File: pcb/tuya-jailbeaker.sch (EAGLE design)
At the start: 17 parts, among them U1 ESP8285, X1 26MHz

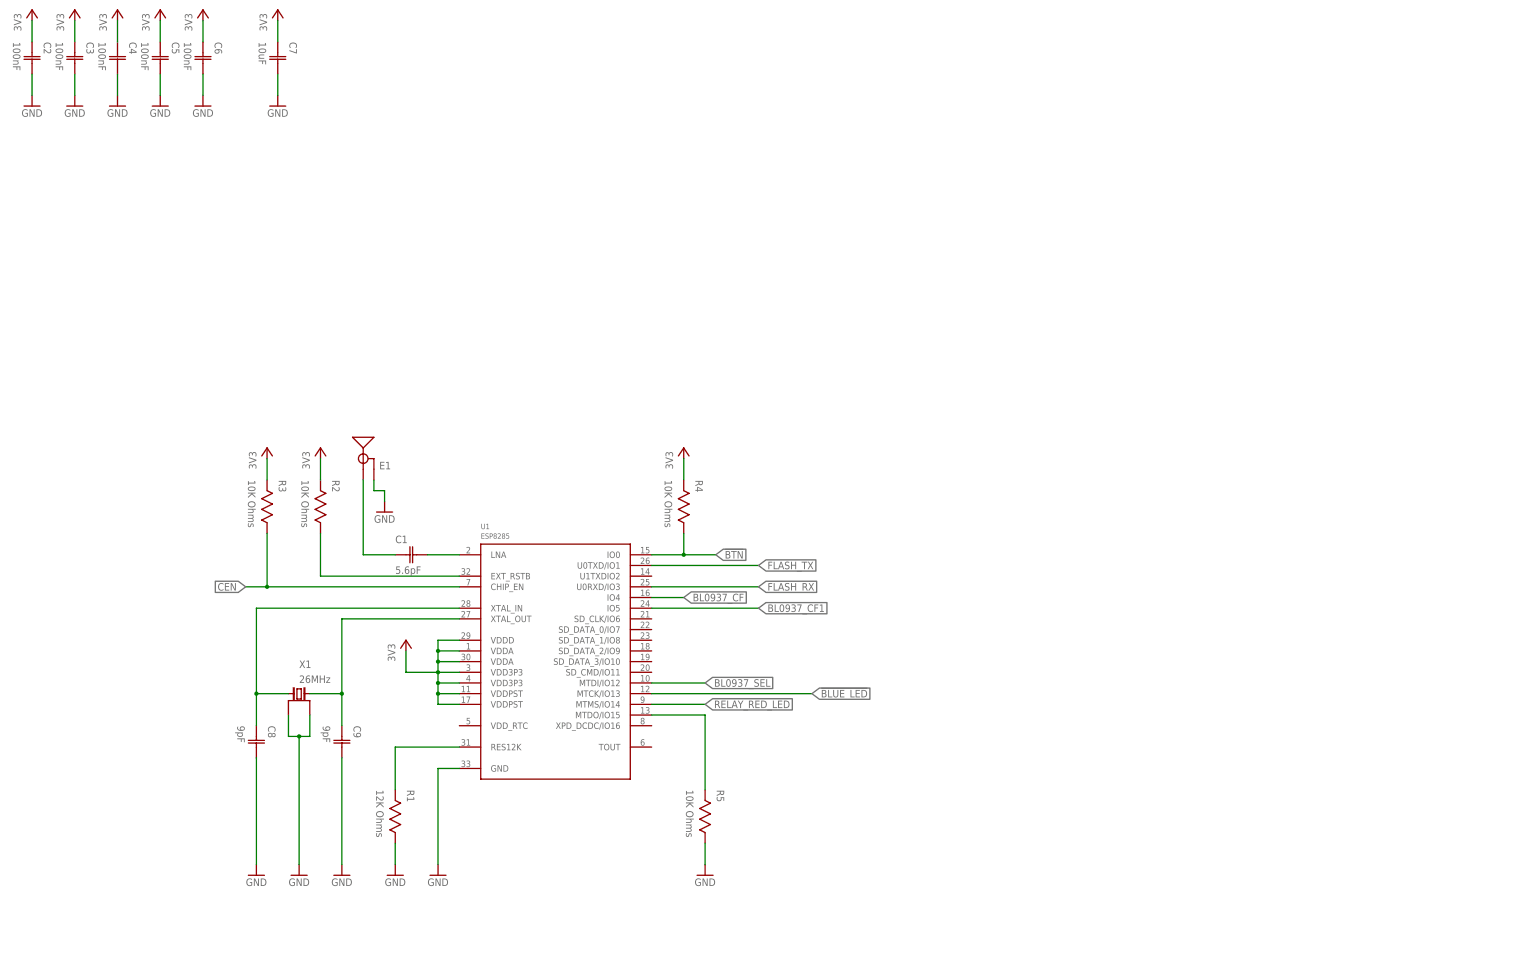
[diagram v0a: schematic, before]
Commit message: Add logo Generate schematic PDF
Signed-off-by: João Silva <jgc3silva@gmail.com>
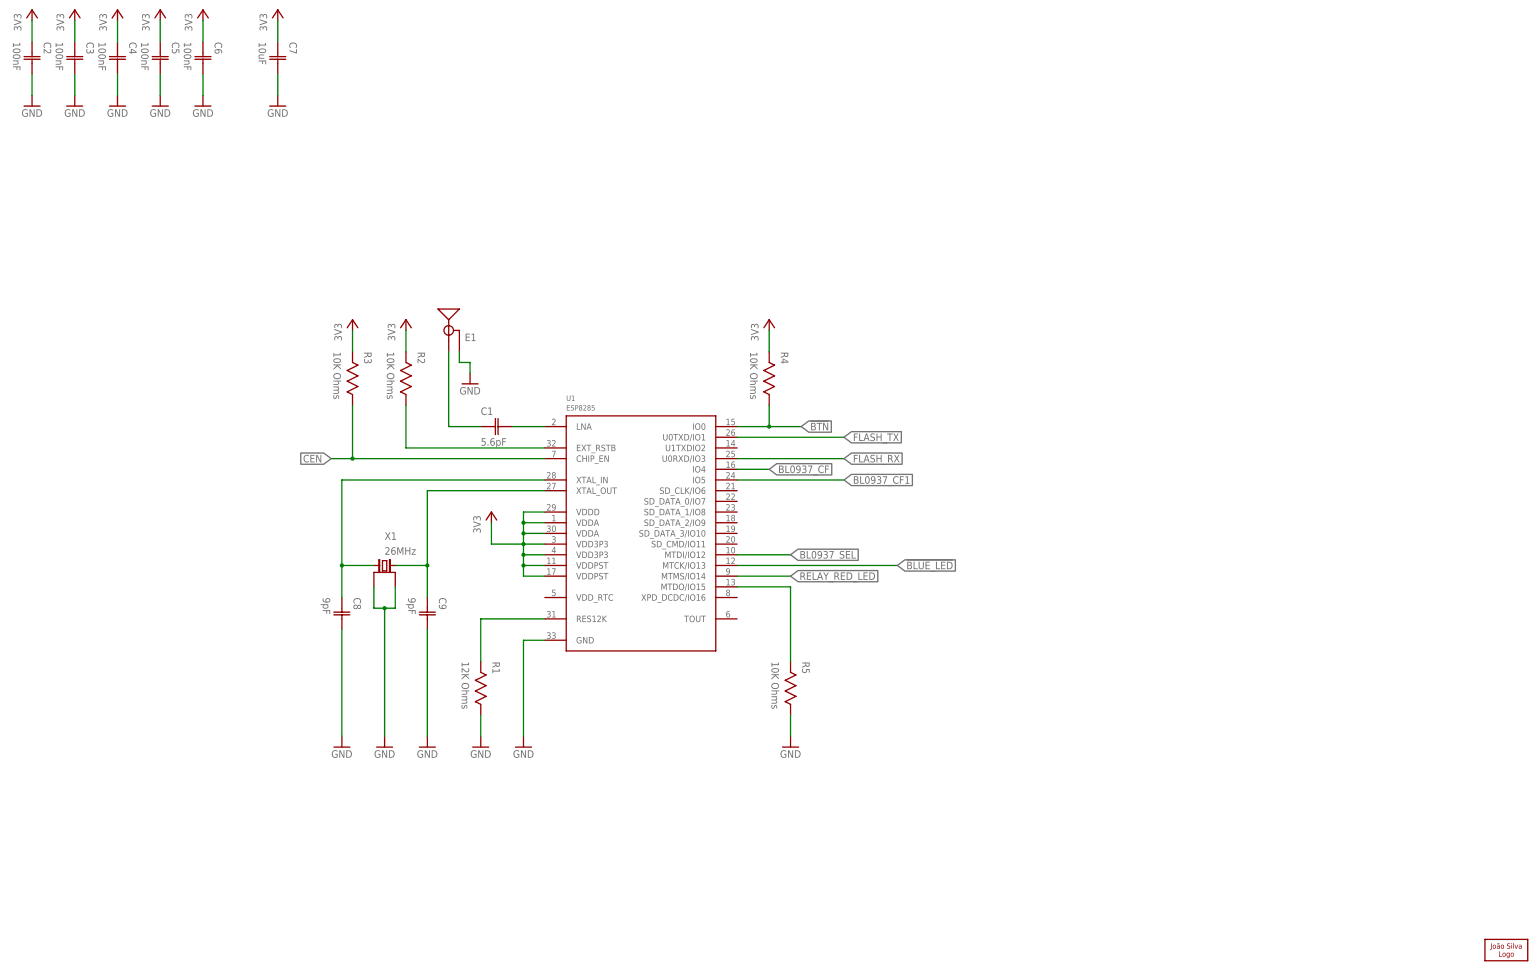
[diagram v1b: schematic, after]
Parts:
- added LOGO1: JS-5MM, Silkscreen:JS-5MM
- X1: OCLCSC (none) -> C709005
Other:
- moved on the sheet: C1, C8, C9, E1, R1, R2, R3, R4, R5, U1, X1

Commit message: Update to ESP32-C3
Signed-off-by: João Silva <jgc3silva@gmail.com>
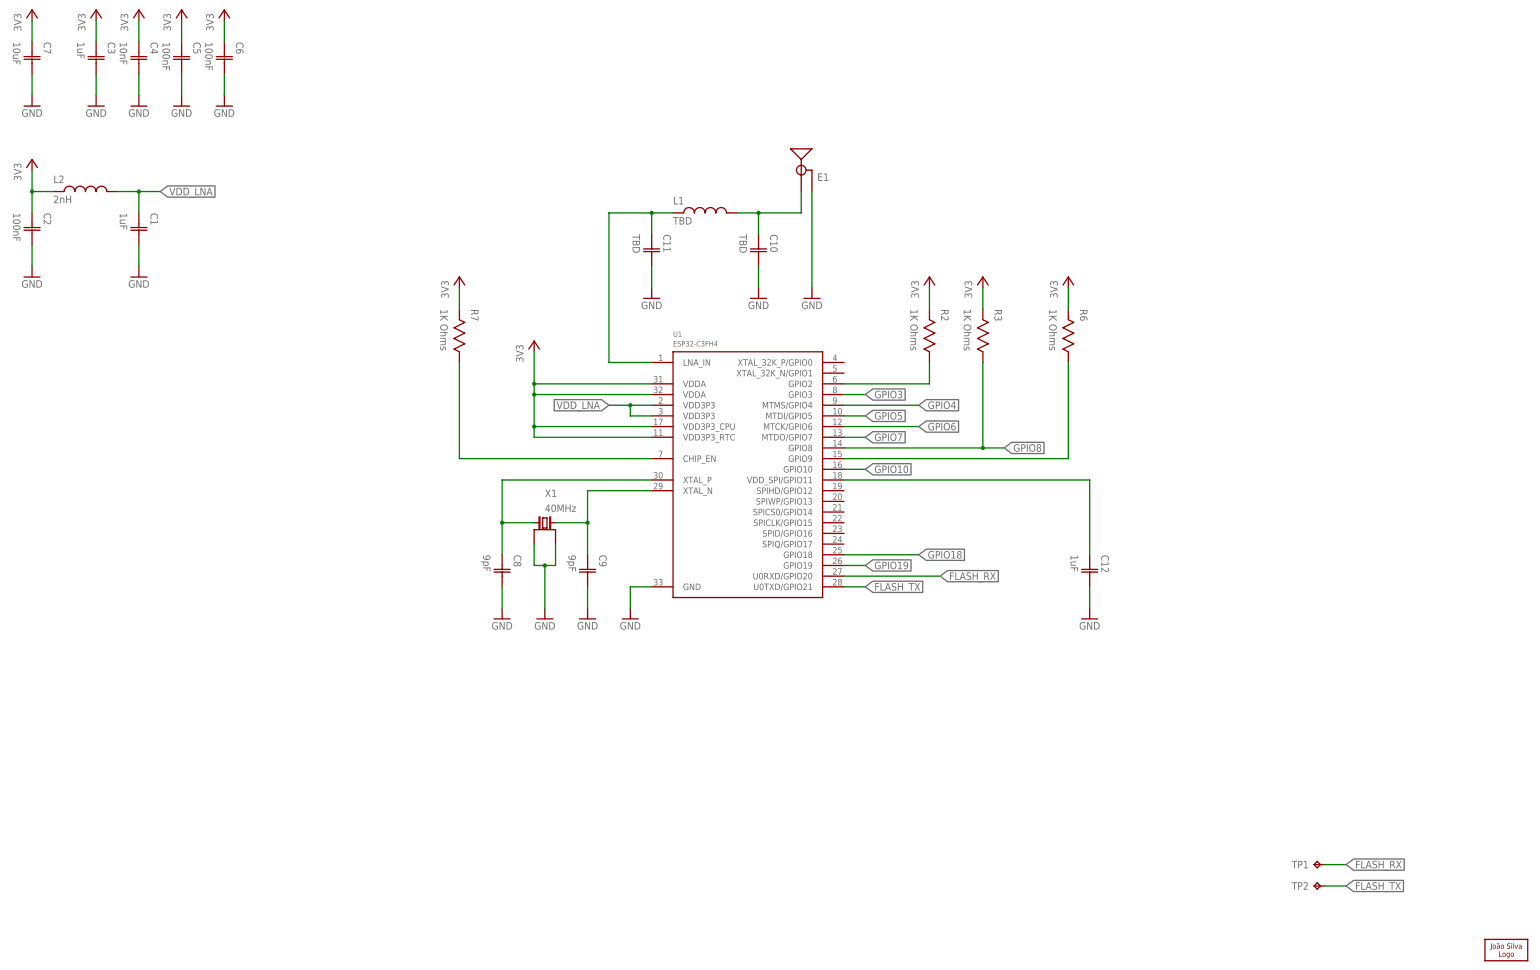
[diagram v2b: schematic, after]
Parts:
- removed R1: 12K Ohms, Resistor:RESISTOR-0201
- removed R4, R5: 10K Ohms, Resistor:RESISTOR-0201
- added C10, C11: TBD, Capacitor:CAPACITOR-0402
- added C12: 1uF, Capacitor:CAPACITOR-0402
- added L1: TBD, Inductor:INDUCTOR-0402
- added L2: 2nH, Inductor:INDUCTOR-0402
- added R6, R7: 1K Ohms, Resistor:RESISTOR-0402
- added TP1, TP2: TESTPOINT-1.27MM, PADs:TESTPOINT-1.27MM
- C1: value 5.6pF -> 1uF; device Capacitor:CAPACITOR-0201 -> Capacitor:CAPACITOR-0402
- C2, C5, C6, C8, C9: device Capacitor:CAPACITOR-0201 -> Capacitor:CAPACITOR-0402
- C3: value 100nF -> 1uF; device Capacitor:CAPACITOR-0201 -> Capacitor:CAPACITOR-0402
- C4: value 100nF -> 10nF; device Capacitor:CAPACITOR-0201 -> Capacitor:CAPACITOR-0402
- R2, R3: value 10K Ohms -> 1K Ohms; device Resistor:RESISTOR-0201 -> Resistor:RESISTOR-0402
- U1: value ESP8285 -> ESP32-C3FH4; device Espressif:ESP8285 -> Espressif:ESP32-C3FH4
- X1: value 26MHz -> 40MHz
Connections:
- removed net !BLUE_LED: U1.MTCK/IO13
- removed net !BTN: R4.1, U1.IO0
- removed net BL0937_CF: U1.IO4
- removed net BL0937_CF1: U1.IO5
- removed net BL0937_SEL: U1.MTDI/IO12
- removed net N$1: C1.C2, U1.LNA
- removed net N$2: C1.C1, E1.SIGNAL
- removed net N$3: R1.2, U1.RES12K
- removed net N$4: R2.1, U1.EXT_RSTB
- removed net N$5: C8.C1, U1.XTAL_IN, X1.1
- removed net N$6: C9.C1, U1.XTAL_OUT, X1.2
- removed net N$7: R5.2, U1.MTDO/IO15
- removed net RELAY_RED_LED: U1.MTMS/IO14
- new net ANT: C10.C1, E1.SIGNAL, L1.2
- new net GPIO10: U1.GPIO10
- new net GPIO18: U1.GPIO18
- new net GPIO19: U1.GPIO19
- new net GPIO2: R2.1, U1.GPIO2
- new net GPIO3: U1.GPIO3
- new net GPIO4: U1.MTMS/GPIO4
- new net GPIO5: U1.MTDI/GPIO5
- new net GPIO6: U1.MTCK/GPIO6
- new net GPIO7: U1.MTDO/GPIO7
- new net GPIO8: R3.1, U1.GPIO8
- new net GPIO9: R6.1, U1.GPIO9
- new net LNA_IN: C11.C1, L1.1, U1.LNA_IN
- new net VDD_LNA: C1.C1, L2.2, U1.VDD3P3@0, U1.VDD3P3@1
- new net VDD_SPI: C12.C1, U1.VDD_SPI/GPIO11
- new net XTALN: C9.C1, U1.XTAL_N, X1.2
- new net XTALP: C8.C1, U1.XTAL_P, X1.1
- net 3V3: now also L2.1, R6.2, R7.2, U1.VDD3P3_CPU, U1.VDD3P3_RTC; no longer R4.2, U1.VDD3P3@0, U1.VDD3P3@1, U1.VDDD, U1.VDDPST@0, U1.VDDPST@1
- net CEN: now also R7.1; no longer R3.1
- net FLASH_RX: now also TP1.TP, U1.U0RXD/GPIO20; no longer U1.U0RXD/IO3
- net FLASH_TX: now also TP2.TP, U1.U0TXD/GPIO21; no longer U1.U0TXD/IO1
- net GND: now also C1.C2, C10.C2, C11.C2, C12.C2; no longer R1.1, R5.1
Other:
- moved on the sheet: C1, C2, C3, C4, C5, C6, C7, C8, C9, E1, R2, R3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
